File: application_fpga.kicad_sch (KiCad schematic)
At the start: 33 parts, among them U6 ICE40UP5K-SG48ITR, U8 SOIC-8

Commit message: V5
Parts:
- removed D3: LED_ARGB, mta1:0402rgb-1010, symbol mta1:FC-B1010RGBT-HG
- added D2: LEDred, LED_SMD:LED_0805_2012Metric_Pad1.15x1.40mm_HandSolder, symbol Device:LED
- added D3: LEDgreen, LED_SMD:LED_0805_2012Metric_Pad1.15x1.40mm_HandSolder, symbol Device:LED
- added D4: LEDblue, LED_SMD:LED_0805_2012Metric_Pad1.15x1.40mm_HandSolder, symbol Device:LED
- C16, C17, C18, C19, C20, C21, C22, C23, C25: footprint C_0805_2012Metric -> Capacitor_SMD:C_0805_2012Metric
- R16, R17, R18, R19, R20, R23, R24, R25, R26: footprint R_0805_2012Metric -> Resistor_SMD:R_0805_2012Metric
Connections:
- net +3.3V: now also D2.2 (A), D3.2 (A), D4.2 (A)
- net at R16.2: now also D2.1 (K)
- net at R17.2: now also D3.1 (K)
- net at R18.2: now also D4.1 (K)
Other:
- moved on the sheet: R16, R17, R18

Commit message: V6
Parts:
- added R4: 10k, Resistor_SMD:R_0805_2012Metric, symbol Device:R
- added SW1: SW_Push, Button_Switch_THT:SW_PUSH_6mm, symbol Switch:SW_Push
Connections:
- net +3.3V: now also SW1.1
- net GND: now also R4.2
- net TOUCH_EVENT: now also R4.1, SW1.2
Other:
- note added: "Touch button"
- note removed: "AHLB 0 1 0 1"
- note removed: "Capacitive sensor"
- note removed: "Mode Syncronous, active high Syncronous, active low Toggle, power-on state = 0 Toggle, power-on state = 1"
- note removed: "Mode setting"
- note removed: "Note: Tune C27 for sensitivity"
- note removed: "TOG 0 0 1 1"

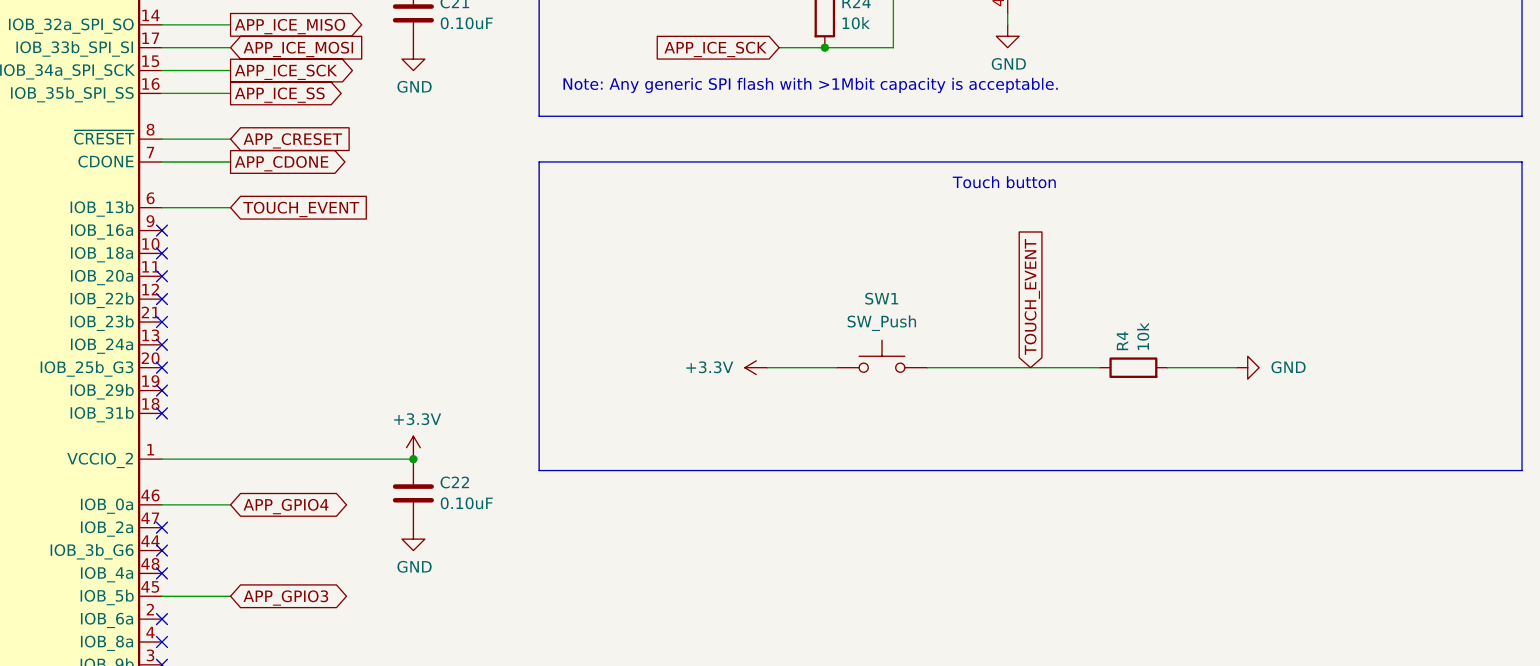
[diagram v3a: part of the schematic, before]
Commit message: Ajout bouton du même style que les projets du LabCyber
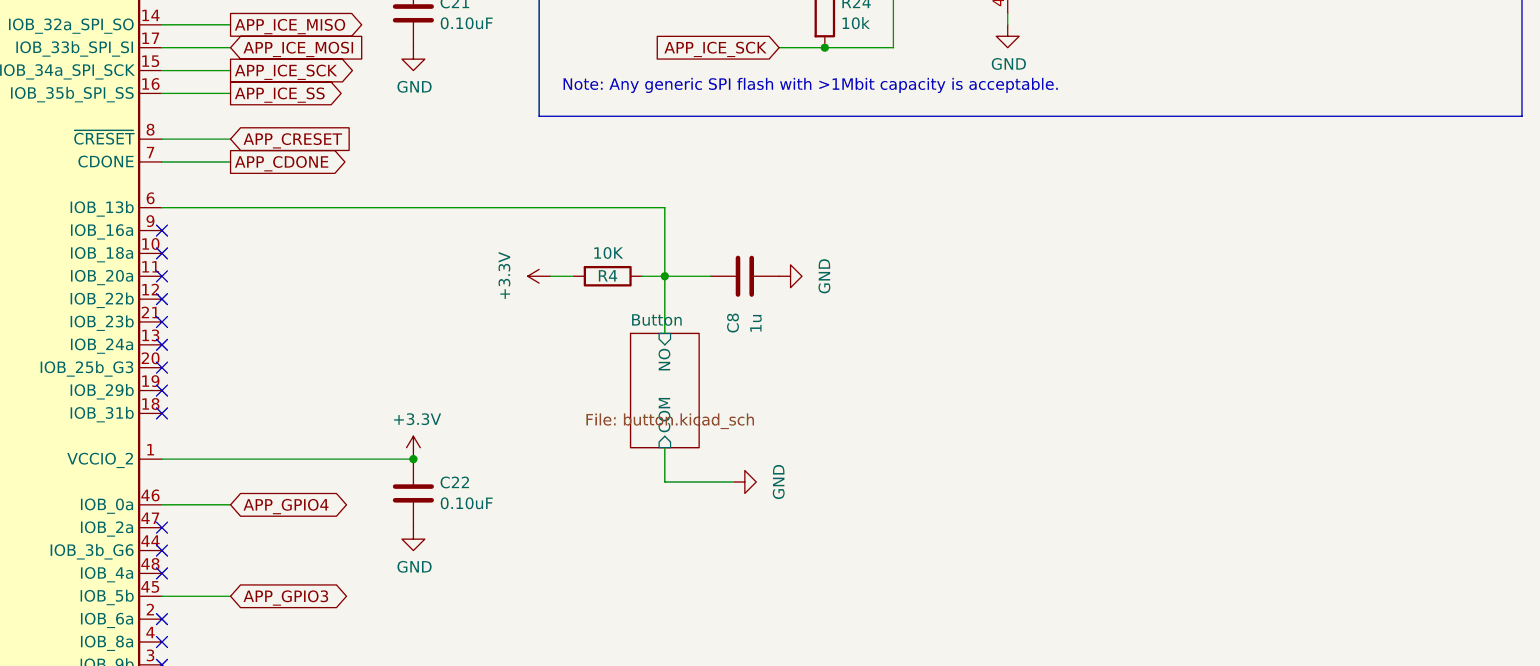
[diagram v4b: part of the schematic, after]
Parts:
- removed SW1: SW_Push, Button_Switch_THT:SW_PUSH_6mm, symbol Switch:SW_Push
- added C8: 1u, Capacitor_SMD:C_0805_2012Metric_Pad1.18x1.45mm_HandSolder, symbol Device:C
- R4: value 10k -> 10K; footprint Resistor_SMD:R_0805_2012Metric -> Resistor_SMD:R_0805_2012Metric_Pad1.20x1.40mm_HandSolder; Extended Value 1/16W,5% -> (none); Manufacturer YAGEO -> (none); Manufacturer Part Number RC0805FR-0710KL -> (none); Mouser Part Number 603-RC0805FR-0710KL -> (none); Supplier Mouser -> (none)
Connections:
- net +3.3V: now also R4.2
- net GND: now also C8.2; no longer R4.2
- net TOUCH_EVENT renamed Button/NO
- net Button/NO: now also C8.1
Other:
- added sheet Button (button.kicad_sch)
- note removed: "Touch button"
